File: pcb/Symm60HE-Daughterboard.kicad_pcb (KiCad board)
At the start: 2 copper layers, 57 x 28 mm, 38 parts, among them J1 TYPE-C-31-M-12, J2 FFC_12P, J3 FFC_12P, SW1 TS-1187A, SW2 TS-1187A, U1 AT32F405RCT7, U2 USBLC6-2SC6, U3 TLV75733PDBV, U4 XC6206P332MR, Y1 12MHz

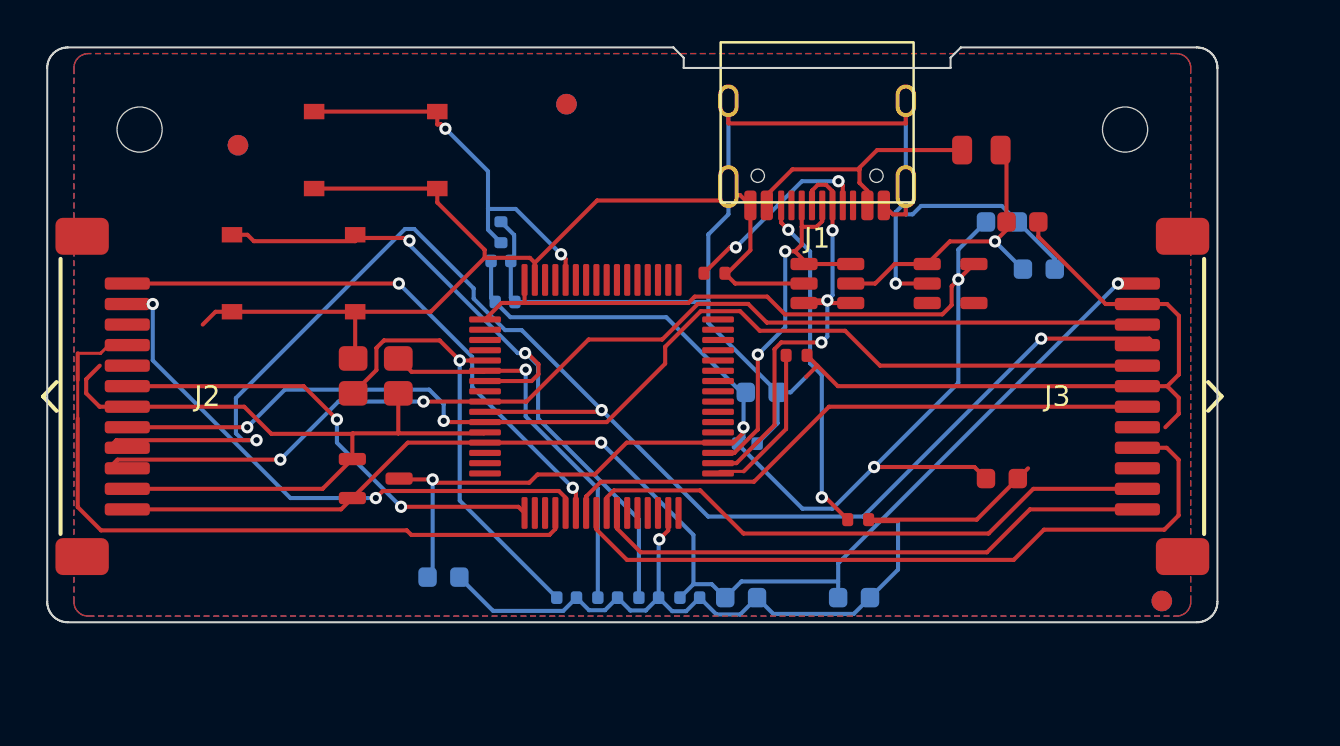
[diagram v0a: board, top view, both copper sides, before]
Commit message: Controller 57 x 27 mm straight rear edge; FPC jumpers into ZIF connectors; Neo Ergo mounting topology
Extend the former local J1 setback across the complete rear edge of the FFC
daughterboard and the Neo controller so the HRO USB-C shell projects 1.0 mm
beyond one straight wall; no component or trace moves. Regenerate all
fabrication releases, panels, Fusion references and renders for the 57 x 27 mm
outline; all twelve DRC reports are clean.

Re-specify the four board interconnects as custom 12-conductor FPC jumpers
with 0.3 mm reinforced same-side tails into the BOOMELE C20111 ZIF connectors
(length TBD from the case route) and update the BOM, READMEs and generators
accordingly. Document that the spring-head modules follow the Neo Ergo
daughterboard mounting topology.

Strip 642 macOS AppleDouble files, rebuild the four JLCPCB and pogo16 Gerber
ZIPs they had been swept into, recompute those checksum lists, and make
release.py and release_pogo16.py skip ._* and .DS_Store like the Neo
generators already do.

Co-Authored-By: Claude Opus 5 <noreply@anthropic.com>
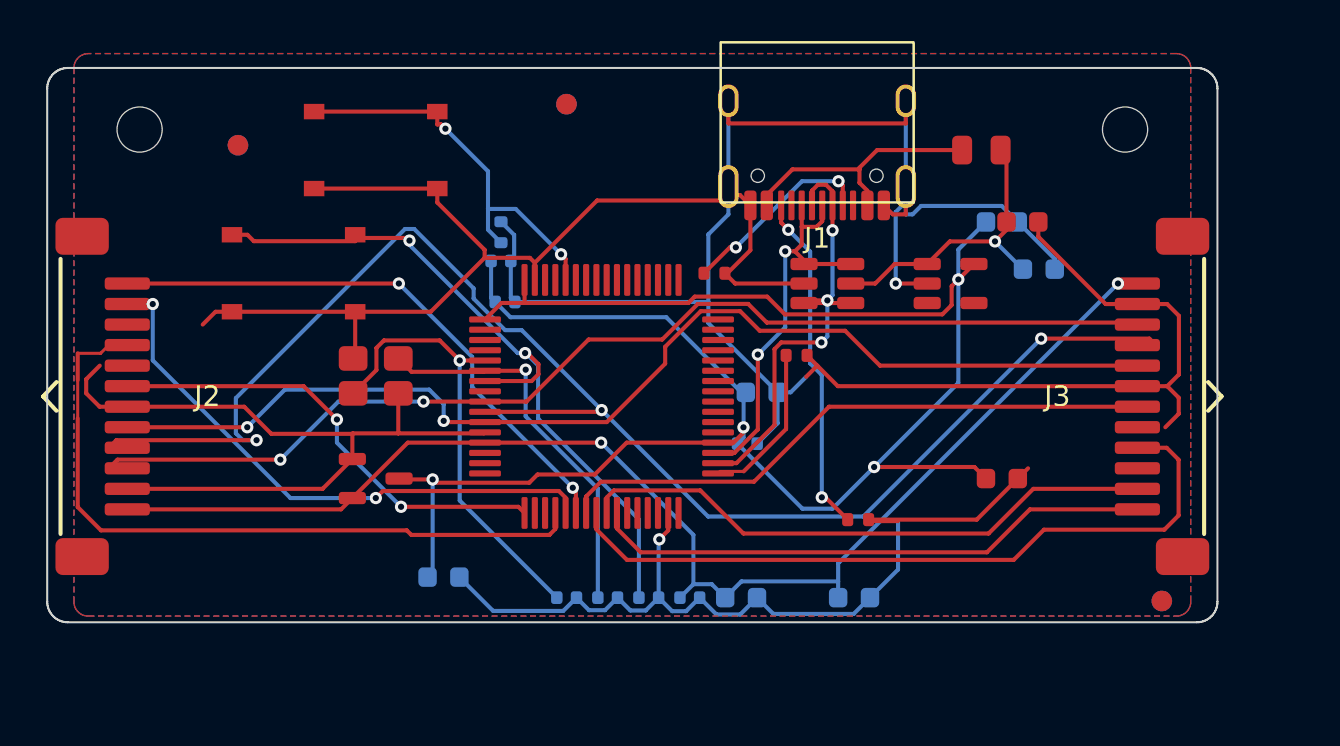
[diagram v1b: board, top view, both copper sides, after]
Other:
- board size 57 x 28 mm -> 57 x 27 mm

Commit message: Replace the project with the reorganised T7 tree: ribbon keyboard is production, pogo archived
Production design is now the outward-facing FPC keyboard with per-key
SK6812MINI-E reverse-mount LEDs, a fifth SN74LV4051A mux per half so every
alternate Hall position has its own channel, an SN74AHCT1G125 LED level
shifter, a 50 x 31 mm daughterboard, 1.5 mm POM plates and 3 degree / 7 degree
tent and typing angles. The universal half panel is fully populated (359
placements) with routed NPTH alignment slots for the mutually exclusive
positions, and eight fixed-layout Left/Right PCB pairs are released under
release/layout-pcbs/ with matching BOM, CPL, Gerber ZIP, drill report and DRC.

Reorganise tools/ into cad/, generators/, layouts/, pcb/, pogo/, releases/ and
rendering/ subpackages; add designs/ and layout/ (KLE) trees and per-layout
gallery renders. The Fusion handoff is a fourteen-body reference STEP with
Gateron KS-20 switch and Cherry-profile keycap references and exact BOOMELE,
HRO and XKB models under case/fusion360/models/official/ with provenance.

The Neo-style pogo variant, its Mill-Max vendor models, the Fusion setup
script and the pogo release packages are archived as design history and
marked DO-NOT-ORDER. Their restored BOM snapshots had reintroduced the wrong
mux part C7792; corrected to C128414 / SN74LV4051ADR and their checksum lists
and archives rebuilt.

Co-Authored-By: Claude Opus 5 <noreply@anthropic.com>
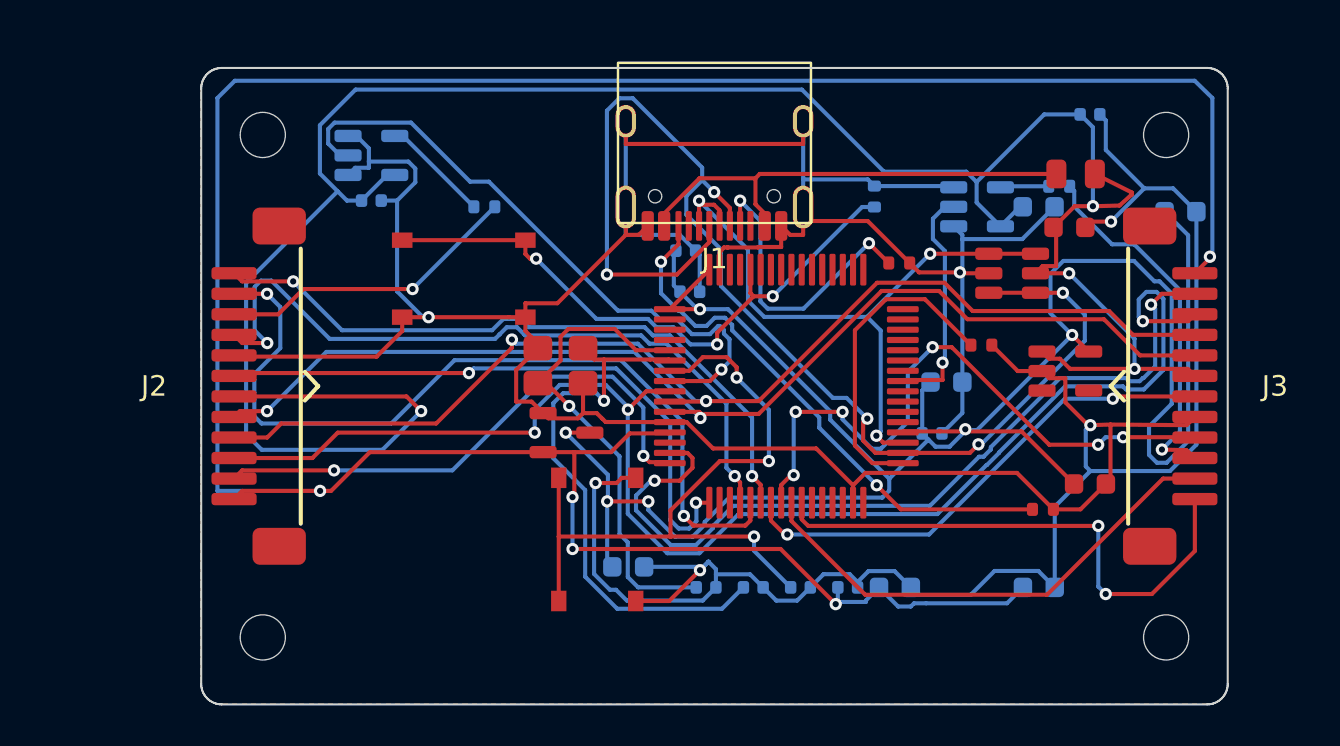
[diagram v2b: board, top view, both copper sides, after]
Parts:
- removed FIDB1, FIDB2, FIDB3: FIDUCIAL_1MM_BCU, Symm60HE_Project:Fiducial_1mm_BCu
- removed FIDF1, FIDF2, FIDF3: FIDUCIAL_1MM_FCU, Symm60HE_Project:Fiducial_1mm_FCu
- added C16: 100n, Symm60HE_Project:C1_C_0402_1005Metric, B.Cu at (170.5, -0.30)
- added C17: 100n, Symm60HE_Project:C1_C_0402_1005Metric, B.Cu at (205.5, -4.50)
- added MHD3: M2_NPTH, Symm60HE_Project:MountingHole_2.2mm_M2_NPTH, F.Cu at (209.2, -3.50)
- added MHD4: M2_NPTH, Symm60HE_Project:MountingHole_2.2mm_M2_NPTH, F.Cu at (165.2, 21.0)
- added R5: 470R, Symm60HE_Project:R3_R_0402_1005Metric, B.Cu at (176.0, 0.00)
- added R6: 470R, Symm60HE_Project:R3_R_0402_1005Metric, B.Cu at (204.0, -1.00)
- added U5: SN74AHCT1G125, Symm60HE_Project:U2_SOT-23-5, B.Cu at (170.5, -2.50)
- added U6: SN74AHCT1G125, Symm60HE_Project:U2_SOT-23-5, B.Cu at (200.0, 0.00)
- moved MHD2 24.8 mm to (209.2, 21.0)
- moved SW2 19.7 mm to (181.5, 16.2), turned to 90 degrees
- moved R4 18.3 mm to (195.0, -0.50)
- moved U4 9.56 mm to (180.0, 11.0)
- moved C14 9.01 mm to (183.0, 17.5)
- moved C15 9.01 mm to (203.0, 18.5)
- moved C5 9.01 mm to (186.0, 4.14)
- moved C6 9.01 mm to (197.8, 11.0)
- moved C7 9.01 mm to (185.8, 2.14)
- moved C8 9.01 mm to (198.5, 8.54)
- moved R1 9.01 mm to (200.2, 6.74)
- moved R2 9.01 mm to (196.2, 2.74)
- moved R3 9.01 mm to (203.2, 14.7)
- moved U1 9.01 mm to (190.7, 8.74)
- moved U2 9.01 mm to (201.7, 3.24)
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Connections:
- J2 pad 1: ADC_L4 -> +3V3A
- J2 pad 10: MUX_A0 -> RGB_L
- J2 pad 11: GND -> ADC_L3
- J2 pad 12: +3V3A -> ADC_L4
- J2 pad 2: ADC_L3 -> ADC_L5
- J2 pad 3: GND -> MUX_A0
- J2 pad 4: ADC_L2 -> MUX_A1
- J2 pad 5: GND -> MUX_A2
- J2 pad 6: ADC_L1 -> VBUS
- J2 pad 7: GND -> ADC_L1
- J2 pad 8: MUX_A2 -> GND
- J2 pad 9: MUX_A1 -> ADC_L2
- J3 pad 1: ADC_R4 -> +3V3A
- J3 pad 10: MUX_A0 -> RGB_R
- J3 pad 11: GND -> ADC_R3
- J3 pad 12: +3V3A -> ADC_R4
- J3 pad 2: ADC_R3 -> ADC_R5
- J3 pad 3: GND -> MUX_A0
- J3 pad 4: ADC_R2 -> MUX_A1
- J3 pad 5: GND -> MUX_A2
- J3 pad 6: ADC_R1 -> VBUS
- J3 pad 7: GND -> ADC_R1
- J3 pad 8: MUX_A2 -> GND
- J3 pad 9: MUX_A1 -> ADC_R2
- U1 pad 15: (no net) -> ADC_R5
- U1 pad 16: (no net) -> ADC_L5
- U1 pad 41: (no net) -> RGB_R_MCU
- U1 pad 8: (no net) -> RGB_L_MCU
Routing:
- net VBUS: track 14.6 -> 114.8 mm, vias 1 -> 4
- net +3V3A: track 65.4 -> 134.5 mm, vias 2 -> 5
- net ADC_R5: track 0.00 -> 41.0 mm, vias 0 -> 2
- net USB_DM: track 22.7 -> 60.9 mm, vias 3 -> 5
- net RGB_L_MCU: track 0.00 -> 30.8 mm, vias 0 -> 1
- net ADC_L5: track 0.00 -> 26.4 mm, vias 0 -> 2
- net MUX_A1: track 74.0 -> 55.5 mm, vias 3 -> 2
- net RGB_R: track 0.00 -> 17.8 mm, vias 0 -> 1
- net RGB_L: track 0.00 -> 14.9 mm, vias 0 -> 1
- net MUX_A0: track 54.7 -> 68.9 mm, vias 2 -> 3
- net USB_DP: track 19.4 -> 32.1 mm, vias 2 -> 3
- net ADC_L3: track 28.8 -> 40.9 mm
- net RGB_R_MCU: track 0.00 -> 11.4 mm, vias 0 -> 1
- net BOOT0: track 19.6 -> 30.0 mm, vias 2 -> 3
- net VBUS_IN: track 12.9 -> 23.0 mm
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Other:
- board size 57 x 27 mm -> 50 x 31 mm
